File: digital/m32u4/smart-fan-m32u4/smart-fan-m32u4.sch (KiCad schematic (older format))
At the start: 31 parts, among them J1 USB_B_Micro, J2 12V, J5 12V, M1 FAN, Q1 BSS138, Q2 BSS138, Q3 SUD19P06-60, U1 LM2936-5.0, U2 LM2936-3.3, U3 ATmega32U4-MU, U4 MAX31826, Y1 16MHz

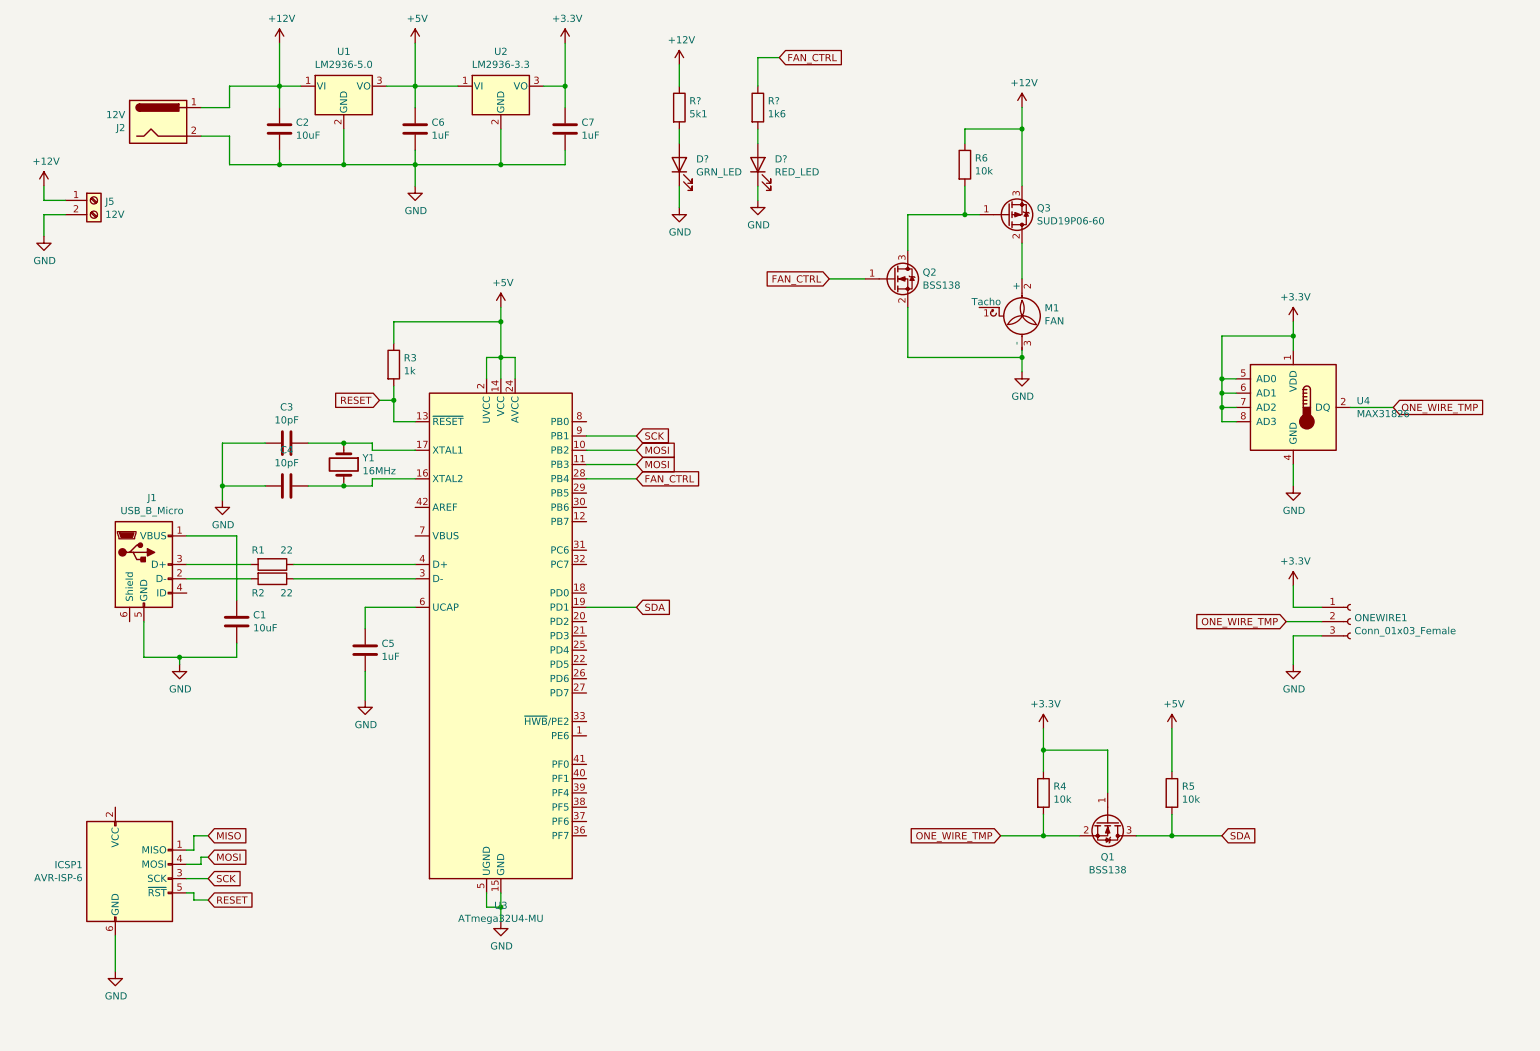
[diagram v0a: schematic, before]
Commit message: Working on layout and adding 2 more fan channels
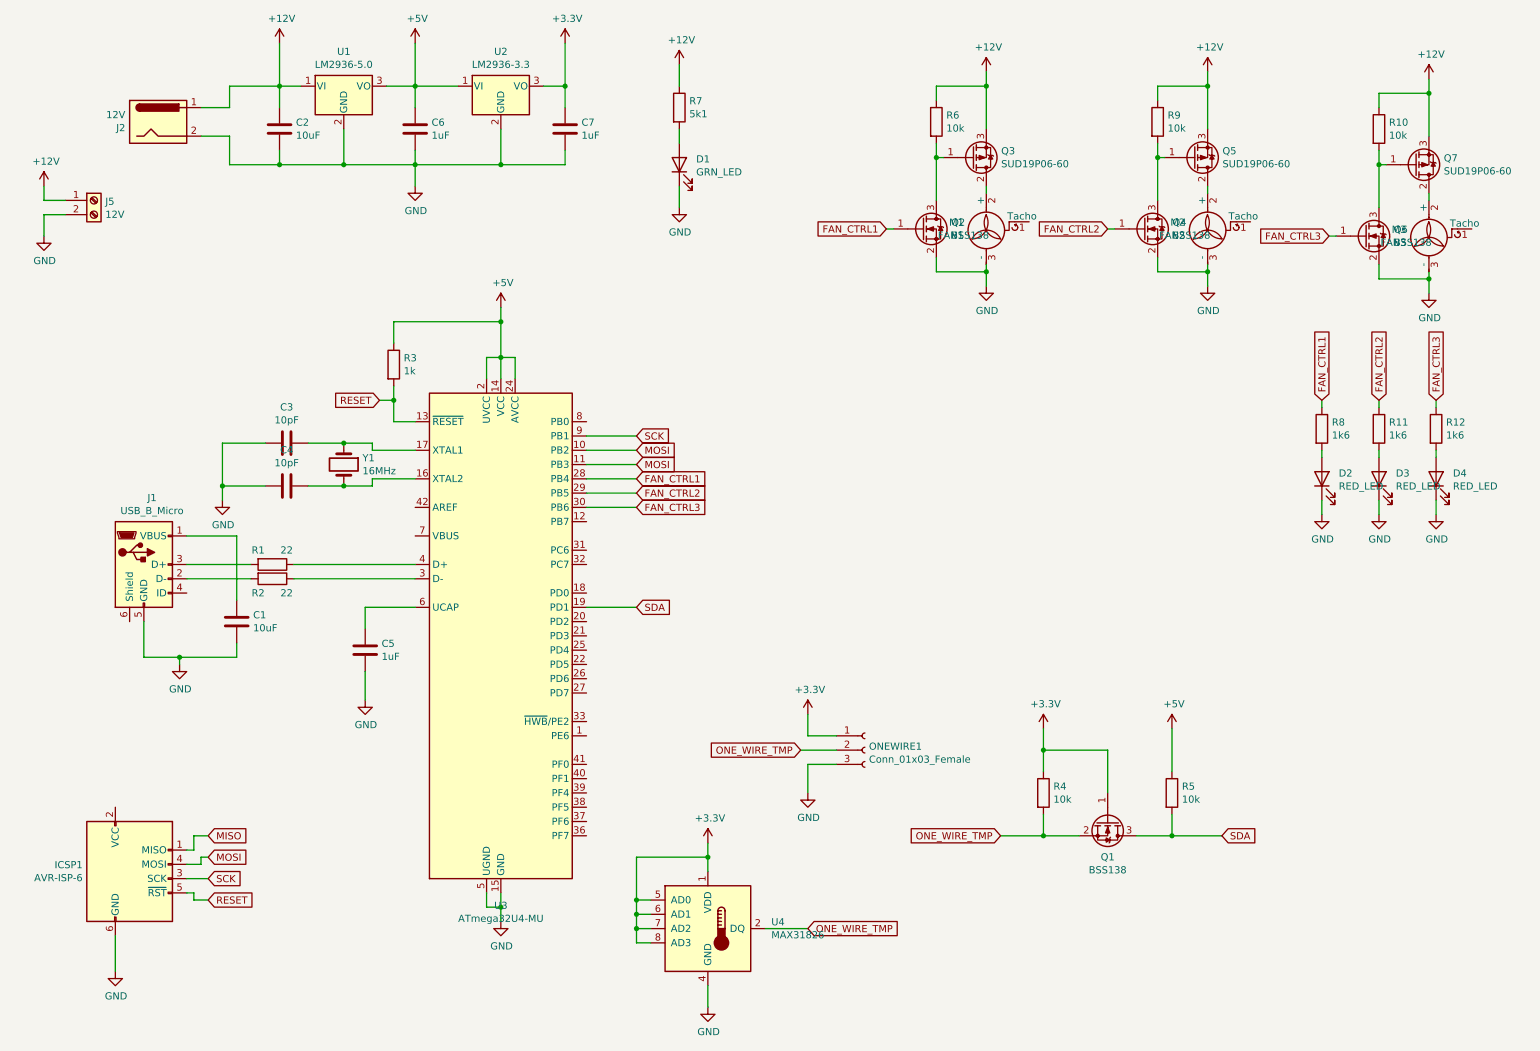
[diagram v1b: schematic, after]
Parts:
- added D3, D4: RED_LED, LED_SMD:LED_0805_2012Metric, symbol Device:LED
- added M2: FAN2, Connector:FanPinHeader_1x03_P2.54mm_Vertical, symbol Motor:Fan_3pin
- added M3: FAN3, Connector:FanPinHeader_1x03_P2.54mm_Vertical, symbol Motor:Fan_3pin
- added Q4, Q6: BSS138, Package_TO_SOT_SMD:SOT-23, symbol Transistor_FET:BSS138
- added Q5, Q7: SUD19P06-60, Package_TO_SOT_SMD:TO-252-2, symbol Transistor_FET:SUD19P06-60
- added R10, R9: 10k, Resistor_SMD:R_0805_2012Metric, symbol Device:R
- added R11, R12: 1k6, Resistor_SMD:R_0805_2012Metric, symbol Device:R
- D1, D2: renamed from D?; footprint (none) -> LED_SMD:LED_0805_2012Metric
- M1: value FAN -> FAN1
- gave numbers to parts that had none: 2
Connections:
- net +12V: now also Q5.3 (S), Q7.3 (S), R10.1, R9.1
- net GND: now also D3.1 (K), D4.1 (K), M2.3 (-), M3.3 (-), Q4.2 (S), Q6.2 (S)
- net FAN_CTRL2: now reaches U3.29 (PB5)
- net FAN_CTRL2: now also Q4.1 (G), R11.1
- net FAN_CTRL3: now reaches U3.30 (PB6)
- net FAN_CTRL3: now also Q6.1 (G), R12.1
- net FAN_CTRL renamed FAN_CTRL1
- new net: Q4.3 (D), Q5.1 (G), R9.2
- new net: M2.2 (+), Q5.2 (D)
- new net: Q6.3 (D), Q7.1 (G), R10.2
- new net: M3.2 (+), Q7.2 (D)
- new net: D3.2 (A), R11.2
- new net: D4.2 (A), R12.2
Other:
- moved on the sheet: D2, M1, ONEWIRE1, Q2, Q3, R6, R8, U4
